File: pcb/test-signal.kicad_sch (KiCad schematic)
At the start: 10 parts, among them J5 731000105, U147 SN74LVC1G3157DCKR, U148 AD5683RARMZ

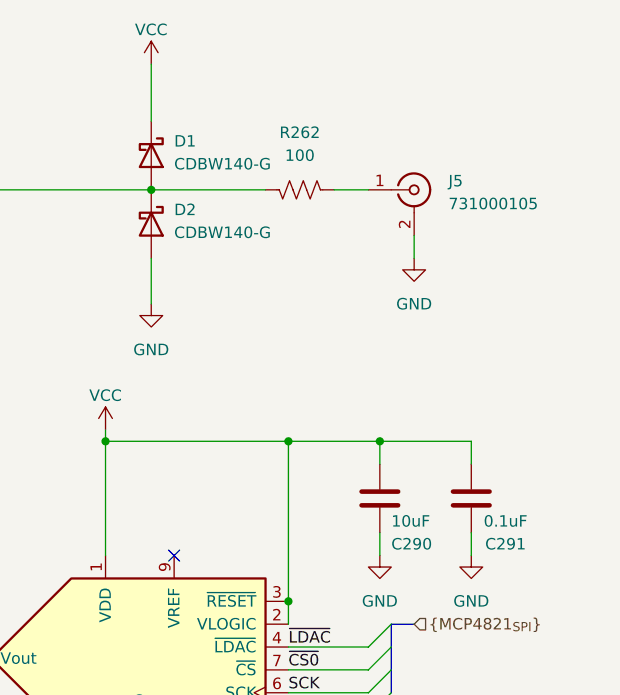
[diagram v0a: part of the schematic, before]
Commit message: 1st step OEPSPN & MPN on components
- still missing new codes to be emitted
- project/schematic/components not tunned with Jon's project at this date
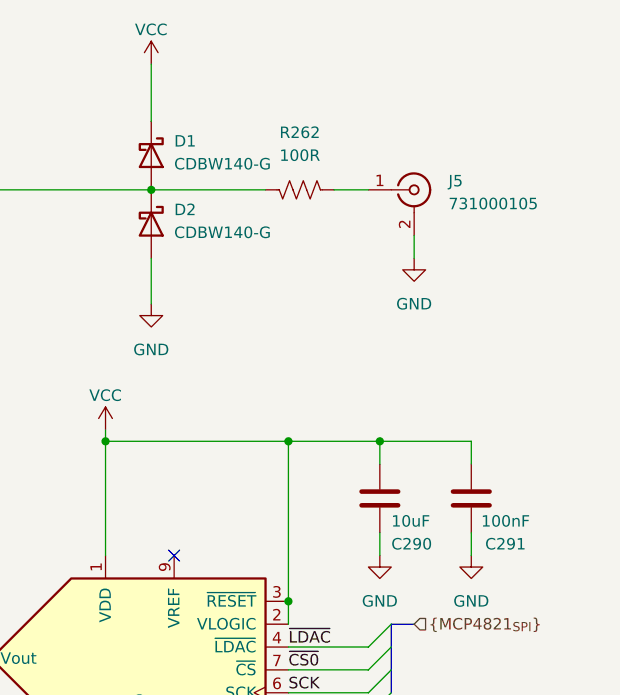
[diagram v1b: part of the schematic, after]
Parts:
- C288: MPN (none) -> GRM155R71E103KA01D; OEPSPN (none) -> OEPS010067
- C290: MPN (none) -> CL31B106KBHNNNE; OEPSPN (none) -> OEPS010032; TempCo X5R -> X7R; Voltage 16V -> 25V
- C291: value 0.1uF -> 100nF; MPN (none) -> C1005X7R1E104K050BB; OEPSPN (none) -> OEPS010050
- D1, D2: MPN (none) -> CDBW140-G; OEPSPN (none) -> espera
- J5: MPN (none) -> 731000105; OEPSPN (none) -> OEPS070024
- R262: value 100 -> 100R; MPN (none) -> TNPW1206100RBEEA; OEPSPN (none) -> OEPS020172
- TP13: now left out of the parts list
- U147: MPN (none) -> SN74LVC1G3157DCKR; OEPSPN (none) -> espera
- U148: MPN (none) -> AD5683RARMZ; OEPSPN (none) -> espera

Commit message: all OEPSPN
- all components with OEPSPN completed
- this Project Fork version not tunned with Project Main Branch
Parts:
- D1, D2: OEPSPN espera -> OEPS030034
- U147: OEPSPN espera -> OEPS080161
- U148: OEPSPN espera -> OEPS080154
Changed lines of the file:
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@@
 			)
 		)
-		(property "OEPSPN" "espera"
+		(property "OEPSPN" "OEPS030034"
 			(at 152.4 67.31 0)
 			(effects
@@
 			)
 		)
-		(property "OEPSPN" "espera"
+		(property "OEPSPN" "OEPS080154"
 			(at 147.32 123.19 0)
 			(effects
@@
 			)
 		)
-		(property "OEPSPN" "espera"
+		(property "OEPSPN" "OEPS080161"
 			(at 111.76 74.93 0)
 			(effects
@@
 			)
 		)
-		(property "OEPSPN" "espera"
+		(property "OEPSPN" "OEPS030034"
 			(at 152.4 74.93 0)
 			(effects

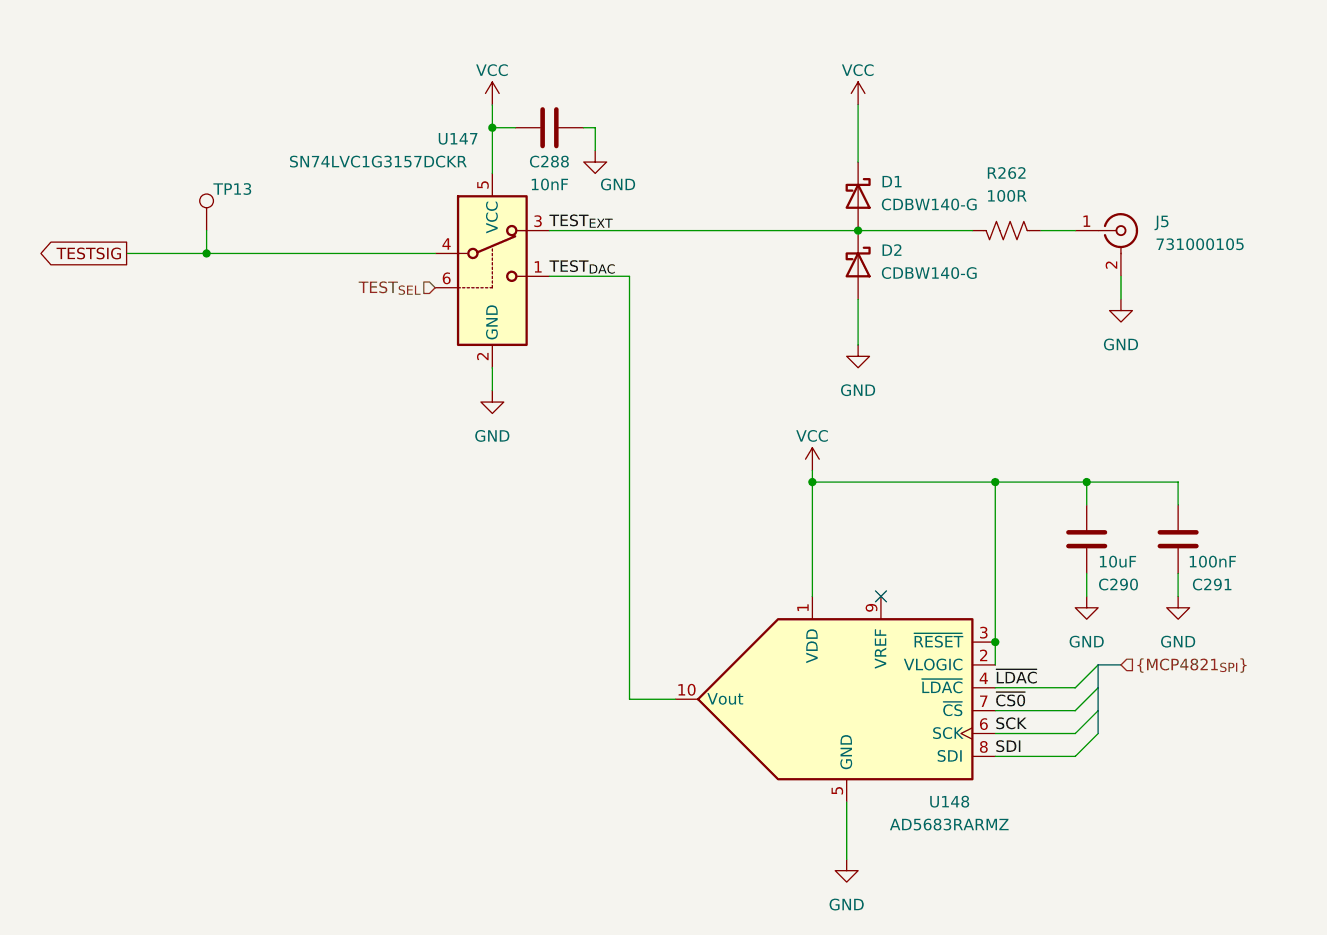
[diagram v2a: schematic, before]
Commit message: tunned with Main branch
- OEPSPN & MPN already on components
- missing 4 these codes
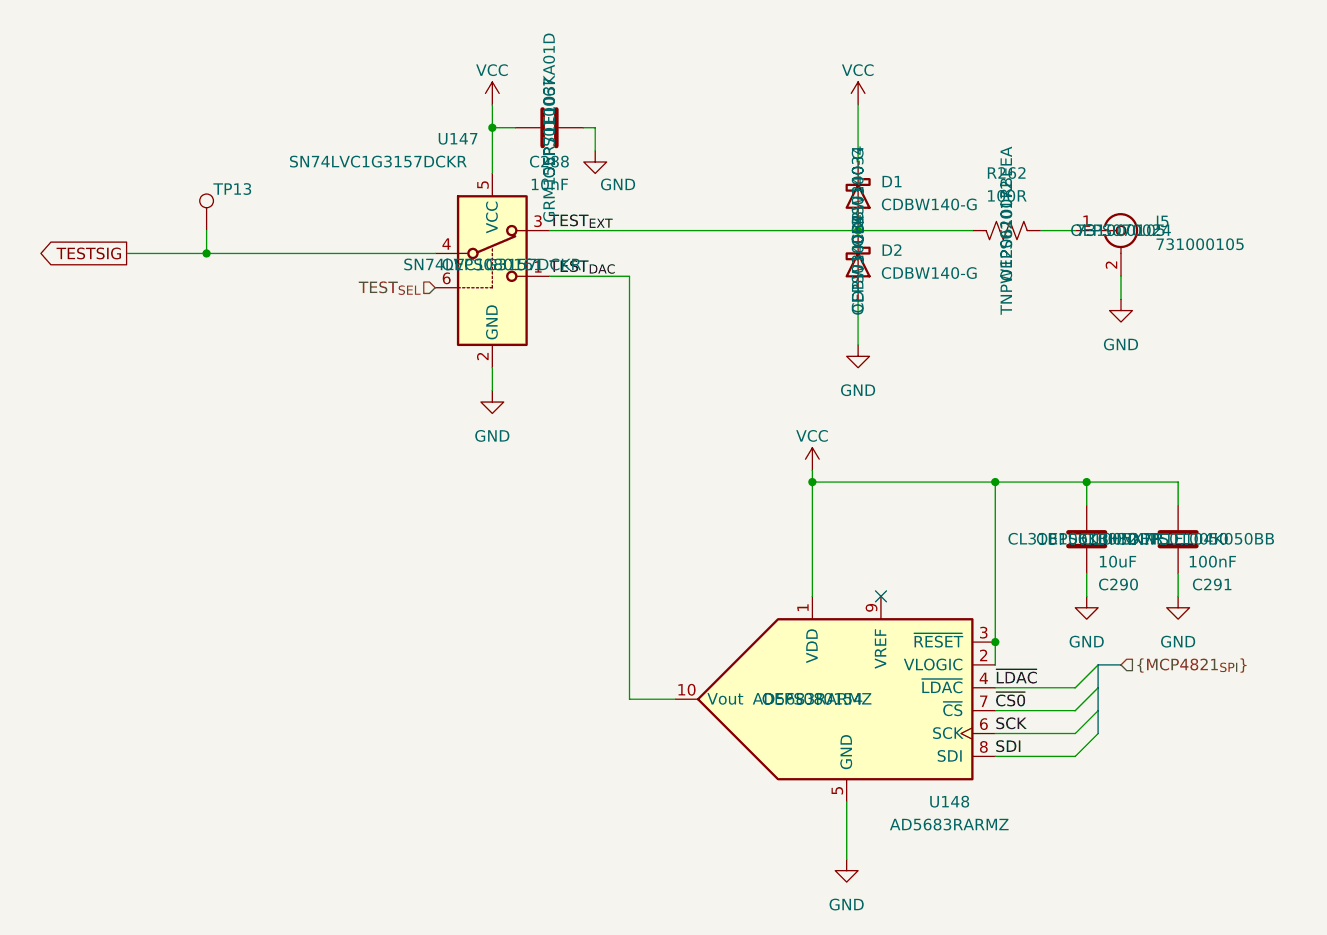
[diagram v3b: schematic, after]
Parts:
- C290: TempCo X7R -> X5R; Voltage 25V -> 16V
